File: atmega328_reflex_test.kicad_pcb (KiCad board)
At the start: 2 copper layers, 100 x 100 mm, 35 parts, among them J1 TM1637, SW1 SW_Keyboard, SW2 SW_Keyboard, SW3 slide_switch, U1 ATmega328-P, Y1 Crystal

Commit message: pcb components laid out
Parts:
- U3: value ~ -> MT3608; moved to F.Cu
- moved R9 123.1 mm to (74.7, 54.0), turned to -90 degrees
- moved R8 121.7 mm to (80.7, 54.0), turned to -90 degrees
- moved R7 120.6 mm to (86.7, 54.0), turned to -90 degrees
- moved R3 112.4 mm to (95.1, 74.0)
- moved R1 96.6 mm to (135.9, 78.0), turned to 0 degrees
- moved STOP 79.4 mm to (118.7, 83.0), turned to -90 degrees
- moved C6 72.2 mm to (139.2, 92.0)
- moved C3 71.9 mm to (138.0, 98.5), turned to -90 degrees
- moved R10 70.0 mm to (122.5, 78.0)
- moved C4 68.8 mm to (141.0, 103.5), turned to 90 degrees
- moved C5 66.9 mm to (144.0, 98.5), turned to -90 degrees
- moved R2 66.0 mm to (112.5, 126.0)
- moved AVG 65.3 mm to (118.7, 90.0), turned to -90 degrees
- moved MULTIPLAYER 61.5 mm to (118.7, 116.0)
- moved R11 60.7 mm to (133.0, 78.0)
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- renumbered D9 to AVG, SW3 to MULTIPLAYER, D10 to STOP

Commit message: initial wiring
changed pin 4 with pin 7
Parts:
- moved U3 31.6 mm to (114.0, 62.5), turned to -90 degrees
- moved R3 7.62 mm to (87.5, 74.0), turned to 0 degrees
- moved C4 5.42 mm to (141.0, 98.1), turned to -90 degrees
- moved C6 1.00 mm to (140.2, 92.0)
- moved C3 0.42 mm to (138.0, 98.1)
- moved C5 0.42 mm to (144.0, 98.1)
- renumbered STOP to D10, AVG to D9, MULTIPLAYER to SW3
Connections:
- C4 pad 1: +5V -> GND
- C4 pad 2: GND -> +5V
- R3 pad 1: Net-(U1-PD7) -> Net-(U1-PD4)
- SW1 pad 1: Net-(U1-PD4) -> Net-(U1-PD7)
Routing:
- net GND: track 0.00 -> 272.7 mm, vias 0 -> 3
- net +5V: track 0.00 -> 100.7 mm, vias 0 -> 1
- net Net-(U1-PD4): track 0.00 -> 47.4 mm, vias 0 -> 1
- net Net-(SW3-B): track 0.00 -> 47.0 mm, vias 0 -> 2
- net Net-(BT1-+): track 0.00 -> 42.0 mm
- net /DIO: track 0.00 -> 41.7 mm, vias 0 -> 3
- net /CLK: track 0.00 -> 39.5 mm, vias 0 -> 1
- net Net-(U1-PD7): track 0.00 -> 37.1 mm
- net Net-(U1-PB2): track 0.00 -> 37.1 mm
- net Net-(U1-PB1): track 0.00 -> 36.1 mm
- net Net-(U1-PB0): track 0.00 -> 35.4 mm
- net Net-(U1-PC0): track 0.00 -> 25.4 mm
- net Net-(U1-PD6): track 0.00 -> 24.2 mm
- net Net-(U1-PC1): track 0.00 -> 16.2 mm
- net Net-(D9-A): track 0.00 -> 16.1 mm
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
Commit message: version 1 finished
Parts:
- added MH1: MountingHole_3.2mm_M3_DIN965, MountingHole:MountingHole_3.2mm_M3_DIN965, F.Cu at (61.0, 53.5)
- added MH2: MountingHole_3.2mm_M3_DIN965, MountingHole:MountingHole_3.2mm_M3_DIN965, F.Cu at (139.0, 53.5)
- added MH3: MountingHole_3.2mm_M3_DIN965, MountingHole:MountingHole_3.2mm_M3_DIN965, F.Cu at (139.0, 146.5)
- added MH4: MountingHole_3.2mm_M3_DIN965, MountingHole:MountingHole_3.2mm_M3_DIN965, F.Cu at (61.0, 146.5)
- SW3: value slide_switch -> MULTIPLAYER
- renumbered U3 to U2
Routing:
- net Net-(U1-PB5): track 0.00 -> 101.1 mm, vias 0 -> 1
- net Net-(U1-PB4): track 0.00 -> 99.2 mm, vias 0 -> 1
- net Net-(U1-PB3): track 0.00 -> 96.6 mm, vias 0 -> 1
- net Net-(U1-PD5): track 0.00 -> 74.1 mm, vias 0 -> 2
- net /DIO: track 41.7 -> 45.1 mm, vias 3 -> 2
- net GND: track 272.7 -> 275.0 mm, vias 3 -> 4
- net Net-(U1-PD4): vias 1 -> 0
- added copper zone on B.Cu, net GND
- added copper zone on F.Cu, net GND
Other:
- outline, holes or cut-outs redrawn
- board text added: "AVERAGE"
- board text added: "SINGLE / MULTI"
- board text added: "STOP"
- board text added: "github.com/KacperBizon/atmega328_reflex_test"
- board text added: "reflex test v1"

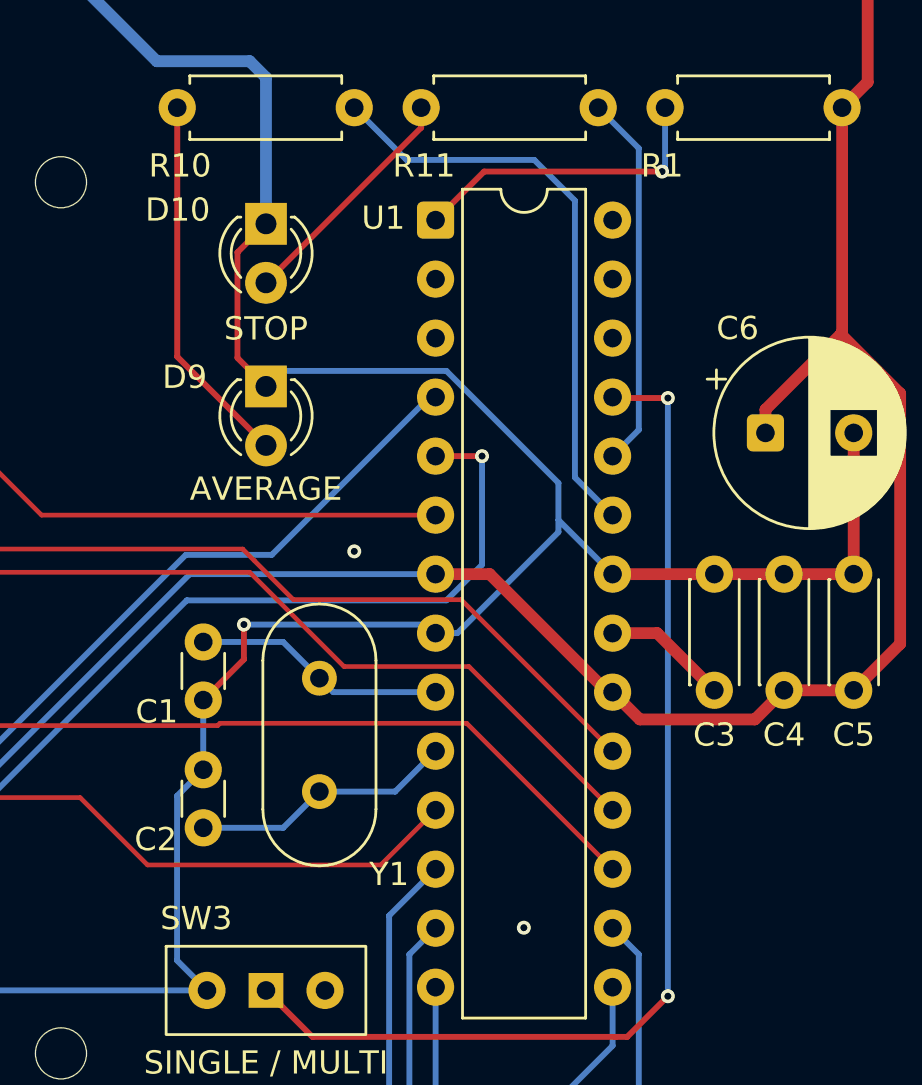
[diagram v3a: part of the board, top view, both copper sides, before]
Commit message: update resistor values
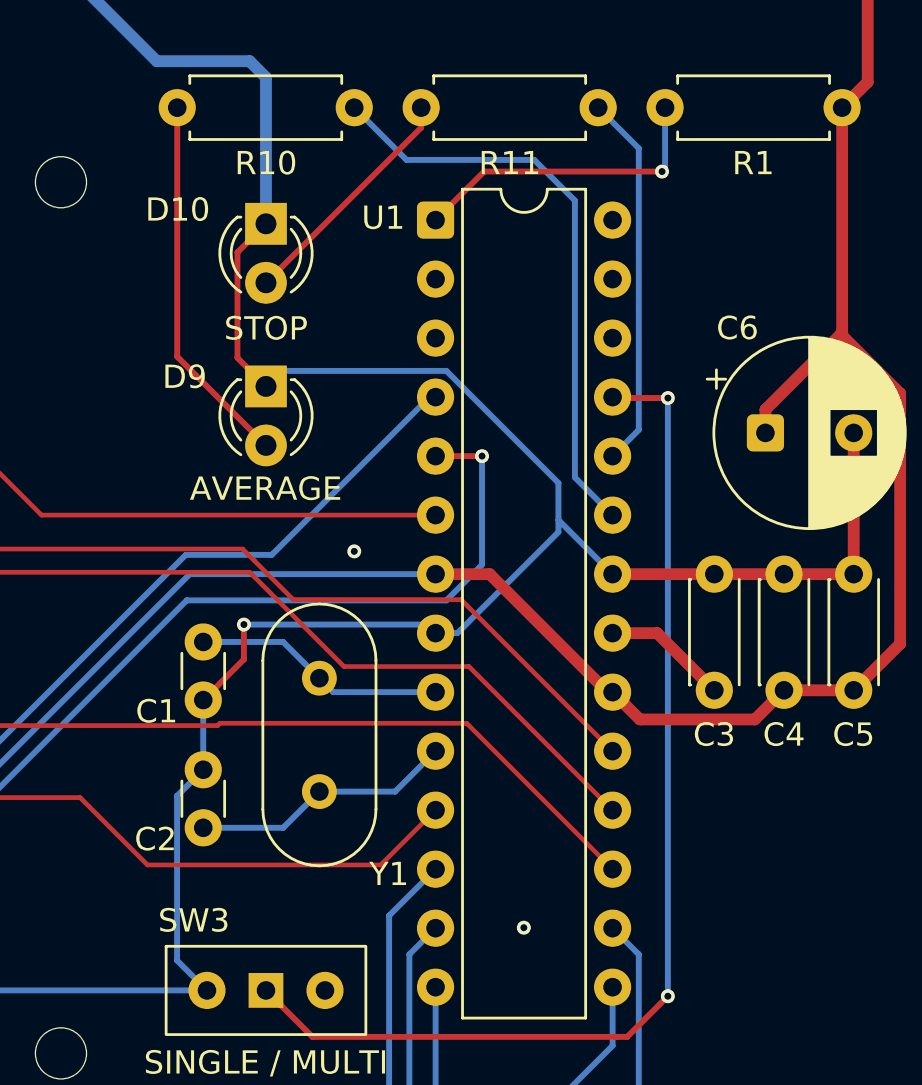
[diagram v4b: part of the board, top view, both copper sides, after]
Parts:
- R10, R11, R4, R5, R6, R7, R8, R9: value 6k8 -> 5k1
- R2, R3: value 4k7 -> 3k3
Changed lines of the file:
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@@
 		)
 		(property "Value" "LED"
-			(at 1.27 2.96 90)
+			(at 1.27 3.5 180)
 			(layer "F.Fab")
 			(effects
@@
 			)
 		)
-		(property "Value" "6k8"
+		(property "Value" "5k1"
 			(at 3.81 2.37 90)
 			(layer "F.Fab")
@@
 		(tags "Resistor Axial_DIN0207 series Axial Horizontal pin pitch 7.62mm 0.25W = 1/4W length 6.3mm diameter 2.5mm")
 		(property "Reference" "R1"
-			(at -0.13 2.5 0)
+			(at 3.8 2.4 0)
 			(layer "F.SilkS")
 			(effects
@@
 		)
 		(property "Value" "10k"
-			(at 3.81 2.37 0)
+			(at 0.32 2.37 0)
 			(layer "F.Fab")
 			(effects
@@
 		(tags "Resistor Axial_DIN0207 series Axial Horizontal pin pitch 7.62mm 0.25W = 1/4W length 6.3mm diameter 2.5mm")
 		(property "Reference" "R10"
-			(at 7.5 -2.5 0)
+			(at 3.8 -2.4 0)
 			(layer "F.SilkS")
 			(effects
@@
 			)
 		)
-		(property "Value" "6k8"
-			(at 4 -2.5 0)
+		(property "Value" "5k1"
+			(at 7.3 -2.4 0)
 			(layer "F.Fab")
 			(effects
@@
 		(tags "switch single-pole opposite-side-connection double-throw SPDT würth wurth")
 		(property "Reference" "SW3"
-			(at -3 -3.1 0)
+			(at -3.1 -3 0)
 			(layer "F.SilkS")
 			(effects
@@
 		)
 		(property "Value" "MULTIPLAYER"
-			(at 0 -3 0)
+			(at 0.1 4.6 0)
 			(layer "F.Fab")
 			(effects
@@
 		)
 		(fp_text user "${REFERENCE}"
-			(at 0 -4 0)
+			(at 2.9 -3 0)
 			(layer "F.Fab")
 			(effects
@@
 		)
 		(property "Value" "LED"
-			(at 1.27 2.96 90)
+			(at 1 3.7 180)
 			(layer "F.Fab")
 			(effects
@@
 		)
 		(fp_text user "${REFERENCE}"
-			(at 34.5 14 270)
+			(at 0.06 6.8 0)
 			(layer "F.Fab")
 			(effects
@@
 		(tags "CP Radial series Radial pin pitch 3.80mm diameter 8mm height 14mm Electrolytic Capacitor")
 		(property "Reference" "C6"
-			(at -1.197349 -4.5 0)
+			(at -1.2 -4.5 0)
 			(layer "F.SilkS")
 			(effects
@@
 		)
 		(property "Value" "10u"
-			(at 1.9 5.25 0)
+			(at 5.6 -4.5 0)
 			(layer "F.Fab")
 			(effects
@@
 			)
 		)
-		(property "Value" "4k7"
+		(property "Value" "3k3"
 			(at 3.81 2.37 0)
 			(layer "F.Fab")
@@
 			)
 		)
-		(property "Value" "6k8"
+		(property "Value" "5k1"
 			(at 3.81 2.37 90)
 			(layer "F.Fab")
@@
 			)
 		)
-		(property "Value" "4k7"
+		(property "Value" "3k3"
 			(at 3.75 -2.25 0)
 			(layer "F.Fab")
@@
 			)
 		)
-		(property "Value" "6k8"
+		(property "Value" "5k1"
 			(at 3.81 2.37 90)
 			(layer "F.Fab")
@@
 		(tags "Resistor Axial_DIN0207 series Axial Horizontal pin pitch 7.62mm 0.25W = 1/4W length 6.3mm diameter 2.5mm")
 		(property "Reference" "R11"
-			(at 7.5 -2.5 0)
+			(at 3.8 -2.4 0)
 			(layer "F.SilkS")
 			(effects
@@
 			)
 		)
-		(property "Value" "6k8"
-			(at 3.5 -2.5 0)
+		(property "Value" "5k1"
+			(at 7.4 -2.4 0)
 			(layer "F.Fab")
 			(effects
@@
 			)
 		)
-		(property "Value" "6k8"
+		(property "Value" "5k1"
 			(at 3.81 2.37 90)
 			(layer "F.Fab")
@@
 			)
 		)
-		(property "Value" "6k8"
+		(property "Value" "5k1"
 			(at 3.81 2.37 90)
 			(layer "F.Fab")
@@
 			)
 		)
-		(property "Value" "6k8"
+		(property "Value" "5k1"
 			(at 3.81 2.37 90)
 			(layer "F.Fab")
